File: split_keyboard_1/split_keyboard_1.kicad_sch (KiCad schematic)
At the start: 64 parts, among them J1 B2B-PH-SM4-TB, SW1 SW_Push_45deg, SW10 SW_Push_45deg, SW11 SW_Push_45deg, SW12 SW_Push_45deg, SW13 SW_Push_45deg, SW14 SW_Push_45deg, SW15 SW_Push_45deg, SW16 SW_Push_45deg, SW17 SW_Push_45deg, SW18 SW_Push_45deg, SW19 SW_Push_45deg, SW2 SW_Push_45deg, SW20 SW_Push_45deg, SW21 SW_Push_45deg, SW22 SW_Push_45deg, SW23 SW_Push_45deg, SW24 SW_Push_45deg, SW25 SW_Push_45deg, SW26 SW_Push_45deg, SW27 SW_Push_45deg, SW28 SW_Push_45deg, SW29 SW_Push_45deg, SW3 SW_Push_45deg, SW30 SW_Push_45deg, SW31 SW_SPDT, SW32 SW_Push, SW4 SW_Push_45deg, SW5 SW_Push_45deg, SW6 SW_Push_45deg, SW7 SW_Push_45deg, SW8 SW_Push_45deg, SW9 SW_Push_45deg

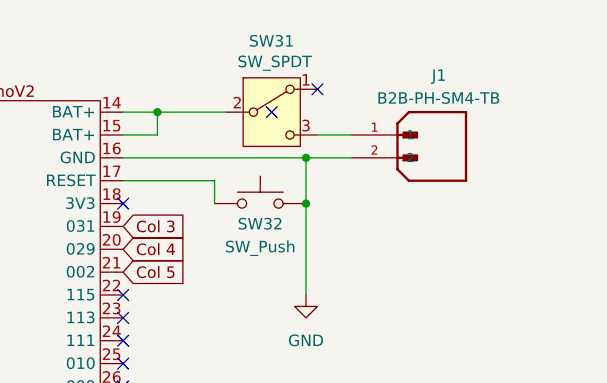
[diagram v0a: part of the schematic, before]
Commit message: on/off switch symbol and start on footprint
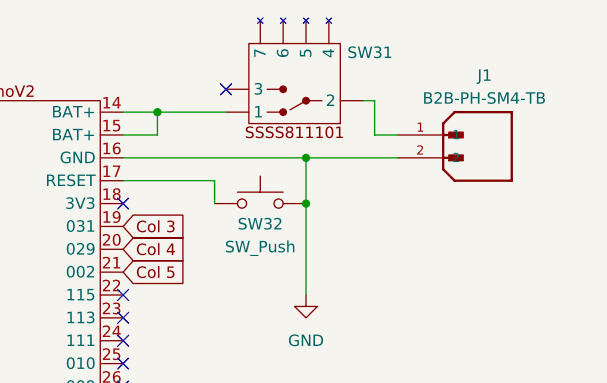
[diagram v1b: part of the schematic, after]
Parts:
- removed SW31: SW_SPDT, symbol Switch:SW_SPDT
- added SW31: ~, symbol schematics:SW_SPDT_SSSS811101
- U1: footprint footprints:nice!nanoV2_reversible -> footprints:nice!nanoV2
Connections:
- net at U1.14 (BAT+), U1.15 (BAT+): now also SW31. (3)
- net at J1.1: now also SW31. (3)
- no-connect marks 16 -> 15
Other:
- moved on the sheet: J1
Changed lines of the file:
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@@
 	)
 	(no_connect
-		(at 248.92 27.94)
+		(at 238.76 27.94)
 	)
 	(no_connect
@@
 	)
 	(no_connect
-		(at 243.84 30.48)
-	)
-	(no_connect
 		(at 196.85 35.56)
 	)
@@
 	(wire
 		(pts
+			(xy 255.27 29.21) (xy 254 29.21)
+		)
+		(stroke
+			(width 0)
+			(type default)
+		)
+	)
+	(wire
+		(pts
 			(xy 82.55 55.88) (xy 82.55 41.91)
 		)
@@
 	(wire
 		(pts
+			(xy 255.27 29.21) (xy 255.27 33.02)
+		)
+		(stroke
+			(width 0)
+			(type default)
+		)
+	)
+	(wire
+		(pts
 			(xy 135.89 99.06) (xy 135.89 120.65)
 		)
@@
 	(wire
 		(pts
-			(xy 252.73 35.56) (xy 247.65 35.56)
+			(xy 257.81 35.56) (xy 247.65 35.56)
 		)
 		(stroke
@@
 	(wire
 		(pts
-			(xy 194.31 38.1) (xy 194.31 40.64)
+			(xy 255.27 33.02) (xy 257.81 33.02)
 		)
 		(stroke
@@
 	(wire
 		(pts
-			(xy 248.92 33.02) (xy 252.73 33.02)
+			(xy 194.31 38.1) (xy 194.31 40.64)
 		)
 		(stroke
@@
 	)
 	(symbol
-		(lib_id "Switch:SW_SPDT")
-		(at 243.84 30.48 0)
-		(unit 1)
-		(exclude_from_sim no)
-		(in_bom yes)
-		(on_board yes)
-		(dnp no)
-		(property "Reference" "SW31"
-			(at 241.3 22.606 0)
-			(effects
-				(font
-					(size 1.27 1.27)
-				)
-				(justify left)
-			)
-		)
-		(property "Value" "SW_SPDT"
-			(at 240.03 24.892 0)
-			(effects
-				(font
-					(size 1.27 1.27)
-				)
-				(justify left)
-			)
-		)
-		(property "Footprint" ""
-			(at 243.84 30.48 0)
-			(effects
-				(font
-					(size 1.27 1.27)
-				)
-				(hide yes)
-			)
-		)
-		(property "Datasheet" "~"
-			(at 243.84 38.1 0)
-			(effects
-				(font
-					(size 1.27 1.27)
-				)
-				(hide yes)
-			)
-		)
-		(property "Description" "Switch, single pole double throw"
-			(at 243.84 30.48 0)
-			(effects
-				(font
-					(size 1.27 1.27)
-				)
-				(hide yes)
-			)
-		)
-		(pin "1"
-		)
-		(pin "2"
-		)
-		(pin "3"
-		)
-		(instances
-			(project ""
-				(path "/dc1d4299-ca53-4805-8c1b-34c27036e41a"
-					(reference "SW31")
-					(unit 1)
-				)
-			)
-		)
-	)
-	(symbol
 		(lib_id "Diode:1N4148W")
 		(at 123.19 64.77 90)
@@
 	)
 	(symbol
+		(lib_id "schematics:SW_SPDT_SSSS811101")
+		(at 246.38 26.67 180)
+		(unit 1)
+		(exclude_from_sim no)
+		(in_bom yes)
+		(on_board yes)
+		(dnp no)
+		(property "Reference" "SW31"
+			(at 254.762 23.876 0)
+			(effects
+				(font
+					(size 1.27 1.27)
+				)
+			)
+		)
+		(property "Value" "~"
+			(at 246.38 38.1 0)
+			(effects
+				(font
+					(size 1.27 1.27)
+				)
+			)
+		)
+		(property "Footprint" ""
+			(at 246.38 26.67 0)
+			(effects
+				(font
+					(size 1.27 1.27)
+				)
+				(hide yes)
+			)
+		)
+		(property "Datasheet" ""
+			(at 246.38 26.67 0)
+			(effects
+				(font
+					(size 1.27 1.27)
+				)
+				(hide yes)
+			)
+		)
+		(property "Description" ""
+			(at 246.38 26.67 0)
+			(effects
+				(font
+					(size 1.27 1.27)
+				)
+				(hide yes)
+			)
+		)
+		(pin ""
+		)
+		(pin ""
+		)
+		(pin ""
+		)
+		(pin ""
+		)
+		(pin ""
+		)
+		(pin ""
+		)
+		(pin ""
+		)
+		(instances
+			(project ""
+				(path "/dc1d4299-ca53-4805-8c1b-34c27036e41a"
+					(reference "SW31")
+					(unit 1)
+				)
+			)
+		)
+	)
+	(symbol
 		(lib_id "Switch:SW_Push_45deg")
 		(at 67.31 146.05 0)
@@
 			)
 		)
-		(property "Footprint" "footprints:nice!nanoV2_reversible"
+		(property "Footprint" "footprints:nice!nanoV2"
 			(at 212.09 44.45 0)
 			(effects
@@
 	(symbol
 		(lib_id "parts:B2B-PH-SM4-TB")
-		(at 261.62 34.29 0)
+		(at 266.7 34.29 0)
 		(unit 1)
 		(exclude_from_sim no)
@@
 		(dnp no)
 		(property "Reference" "J1"
-			(at 261.62 26.416 0)
+			(at 266.7 26.416 0)
 			(effects
 				(font
@@
 		)
 		(property "Value" "B2B-PH-SM4-TB"
-			(at 255.524 28.956 0)
+			(at 260.604 28.956 0)
 			(effects
 				(font
@@
 		)
 		(property "Footprint" "B2B-PH-SM4-TB:JST_B2B-PH-SM4-TB"
-			(at 261.62 34.29 0)
+			(at 266.7 34.29 0)
 			(effects
 				(font
@@
 		)
 		(property "Datasheet" ""
-			(at 261.62 34.29 0)
+			(at 266.7 34.29 0)
 			(effects
 				(font
@@
 		)
 		(property "Description" ""
-			(at 261.62 34.29 0)
+			(at 266.7 34.29 0)
 			(effects
 				(font
@@
 		)
 		(property "MF" "JST"
-			(at 260.858 34.29 0)
+			(at 265.938 34.29 0)
 			(effects
 				(font
@@
 		)
 		(property "MAXIMUM_PACKAGE_HEIGHT" "6.6 mm"
-			(at 261.62 34.036 0)
+			(at 266.7 34.036 0)
 			(effects
 				(font
@@
 		)
 		(property "Package" "NON STANDARD-2 JST"
-			(at 259.334 34.29 0)
+			(at 264.414 34.29 0)
 			(effects
 				(font
@@
 		)
 		(property "Price" "None"
-			(at 260.858 34.29 0)
+			(at 265.938 34.29 0)
 			(effects
 				(font
@@
 		)
 		(property "Check_prices" "https://www.snapeda.com/parts/B2B-PH-SM4-TB/JST/view-part/?ref=eda"
-			(at 261.62 34.29 0)
+			(at 266.7 34.29 0)
 			(effects
 				(font
@@
 		)
 		(property "STANDARD" "Manufacturer Recommendations"
-			(at 261.62 34.29 0)
+			(at 266.7 34.29 0)
 			(effects
 				(font
@@
 		)
 		(property "PARTREV" "N/A"
-			(at 260.858 34.29 0)
+			(at 265.938 34.29 0)
 			(effects
 				(font
@@
 		)
 		(property "SnapEDA_Link" "https://www.snapeda.com/parts/B2B-PH-SM4-TB/JST/view-part/?ref=snap"
-			(at 261.62 34.29 0)
+			(at 266.7 34.29 0)
 			(effects
 				(font
@@
 		)
 		(property "MP" "B2B-PH-SM4-TB"
-			(at 259.334 34.29 0)
+			(at 264.414 34.29 0)
 			(effects
 				(font
@@
 		)
 		(property "Description_1" "Connector Header Surface Mount 2 position 0.079 (2.00mm)"
-			(at 261.62 34.29 0)
+			(at 266.7 34.29 0)
 			(effects
 				(font
@@
 		)
 		(property "Availability" "In Stock"
-			(at 260.604 34.036 0)
+			(at 265.684 34.036 0)
 			(effects
 				(font
@@
 		)
 		(property "MANUFACTURER" "JST"
-			(at 263.652 34.29 0)
+			(at 268.732 34.29 0)
 			(effects
 				(font

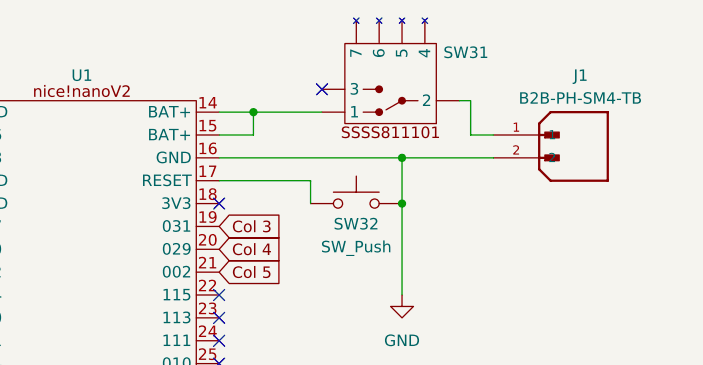
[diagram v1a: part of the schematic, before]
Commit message: Add reset and power switch
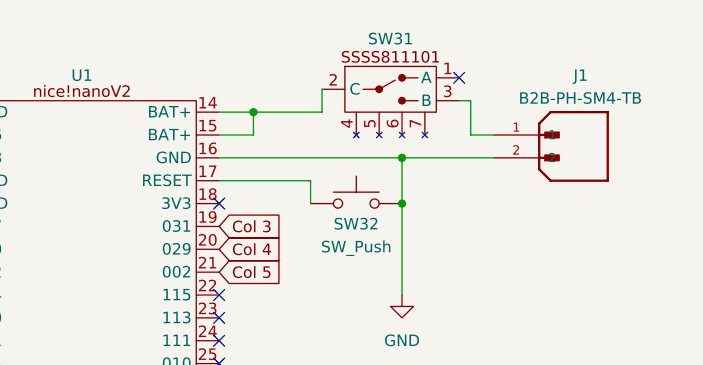
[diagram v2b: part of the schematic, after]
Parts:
- J1: footprint B2B-PH-SM4-TB:JST_B2B-PH-SM4-TB -> Connector_JST:JST_GH_SM02B-GHS-TB_1x02-1MP_P1.25mm_Horizontal
- SW31: footprint (none) -> footprints:SSSS811101_SW_SPDT
- SW32: footprint (none) -> footprints:EVQPU_BTN
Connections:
- net at U1.14 (BAT+), U1.15 (BAT+): now also SW31.2 (C); no longer SW31. (3)
- net at J1.1: now also SW31.3 (B); no longer SW31. (3)
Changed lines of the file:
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@@
 	)
 	(no_connect
-		(at 238.76 27.94)
-	)
-	(no_connect
 		(at 210.82 68.58)
 	)
@@
 	)
 	(no_connect
+		(at 254 26.67)
+	)
+	(no_connect
 		(at 196.85 35.56)
 	)
@@
 	(wire
 		(pts
+			(xy 238.76 27.94) (xy 238.76 30.48)
+		)
+		(stroke
+			(width 0)
+			(type default)
+		)
+	)
+	(wire
+		(pts
 			(xy 52.07 156.21) (xy 69.85 156.21)
 		)
@@
 			)
 		)
-		(property "Footprint" ""
+		(property "Footprint" "footprints:EVQPU_BTN"
 			(at 242.57 35.56 0)
 			(effects
@@
 	)
 	(symbol
-		(lib_id "schematics:SW_SPDT_SSSS811101")
-		(at 246.38 26.67 180)
-		(unit 1)
-		(exclude_from_sim no)
-		(in_bom yes)
-		(on_board yes)
-		(dnp no)
-		(property "Reference" "SW31"
-			(at 254.762 23.876 0)
-			(effects
-				(font
-					(size 1.27 1.27)
-				)
-			)
-		)
-		(property "Value" "~"
-			(at 246.38 38.1 0)
-			(effects
-				(font
-					(size 1.27 1.27)
-				)
-			)
-		)
-		(property "Footprint" ""
-			(at 246.38 26.67 0)
-			(effects
-				(font
-					(size 1.27 1.27)
-				)
-				(hide yes)
-			)
-		)
-		(property "Datasheet" ""
-			(at 246.38 26.67 0)
-			(effects
-				(font
-					(size 1.27 1.27)
-				)
-				(hide yes)
-			)
-		)
-		(property "Description" ""
-			(at 246.38 26.67 0)
-			(effects
-				(font
-					(size 1.27 1.27)
-				)
-				(hide yes)
-			)
-		)
-		(pin ""
-		)
-		(pin ""
-		)
-		(pin ""
-		)
-		(pin ""
-		)
-		(pin ""
-		)
-		(pin ""
-		)
-		(pin ""
-		)
-		(instances
-			(project ""
-				(path "/dc1d4299-ca53-4805-8c1b-34c27036e41a"
-					(reference "SW31")
-					(unit 1)
-				)
-			)
-		)
-	)
-	(symbol
 		(lib_id "Switch:SW_Push_45deg")
 		(at 67.31 146.05 0)
@@
 	)
 	(symbol
+		(lib_id "schematics:SW_SPDT_SSSS811101")
+		(at 246.38 30.48 0)
+		(unit 1)
+		(exclude_from_sim no)
+		(in_bom yes)
+		(on_board yes)
+		(dnp no)
+		(property "Reference" "SW31"
+			(at 246.38 22.352 0)
+			(effects
+				(font
+					(size 1.27 1.27)
+				)
+			)
+		)
+		(property "Value" "~"
+			(at 246.38 21.59 0)
+			(effects
+				(font
+					(size 1.27 1.27)
+				)
+			)
+		)
+		(property "Footprint" "footprints:SSSS811101_SW_SPDT"
+			(at 246.38 30.48 0)
+			(effects
+				(font
+					(size 1.27 1.27)
+				)
+				(hide yes)
+			)
+		)
+		(property "Datasheet" ""
+			(at 246.38 30.48 0)
+			(effects
+				(font
+					(size 1.27 1.27)
+				)
+				(hide yes)
+			)
+		)
+		(property "Description" ""
+			(at 246.38 30.48 0)
+			(effects
+				(font
+					(size 1.27 1.27)
+				)
+				(hide yes)
+			)
+		)
+		(pin "6"
+		)
+		(pin "4"
+		)
+		(pin "5"
+		)
+		(pin "7"
+		)
+		(pin "2"
+		)
+		(pin "3"
+		)
+		(pin "1"
+		)
+		(instances
+			(project ""
+				(path "/dc1d4299-ca53-4805-8c1b-34c27036e41a"
+					(reference "SW31")
+					(unit 1)
+				)
+			)
+		)
+	)
+	(symbol
 		(lib_id "Diode:1N4148W")
 		(at 69.85 107.95 90)
@@
 			)
 		)
-		(property "Footprint" "B2B-PH-SM4-TB:JST_B2B-PH-SM4-TB"
+		(property "Footprint" "Connector_JST:JST_GH_SM02B-GHS-TB_1x02-1MP_P1.25mm_Horizontal"
 			(at 266.7 34.29 0)
 			(effects
